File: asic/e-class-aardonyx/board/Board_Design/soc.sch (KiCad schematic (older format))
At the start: 111 parts, among them SW3 SW_DIP_x03, U15 SKT32E

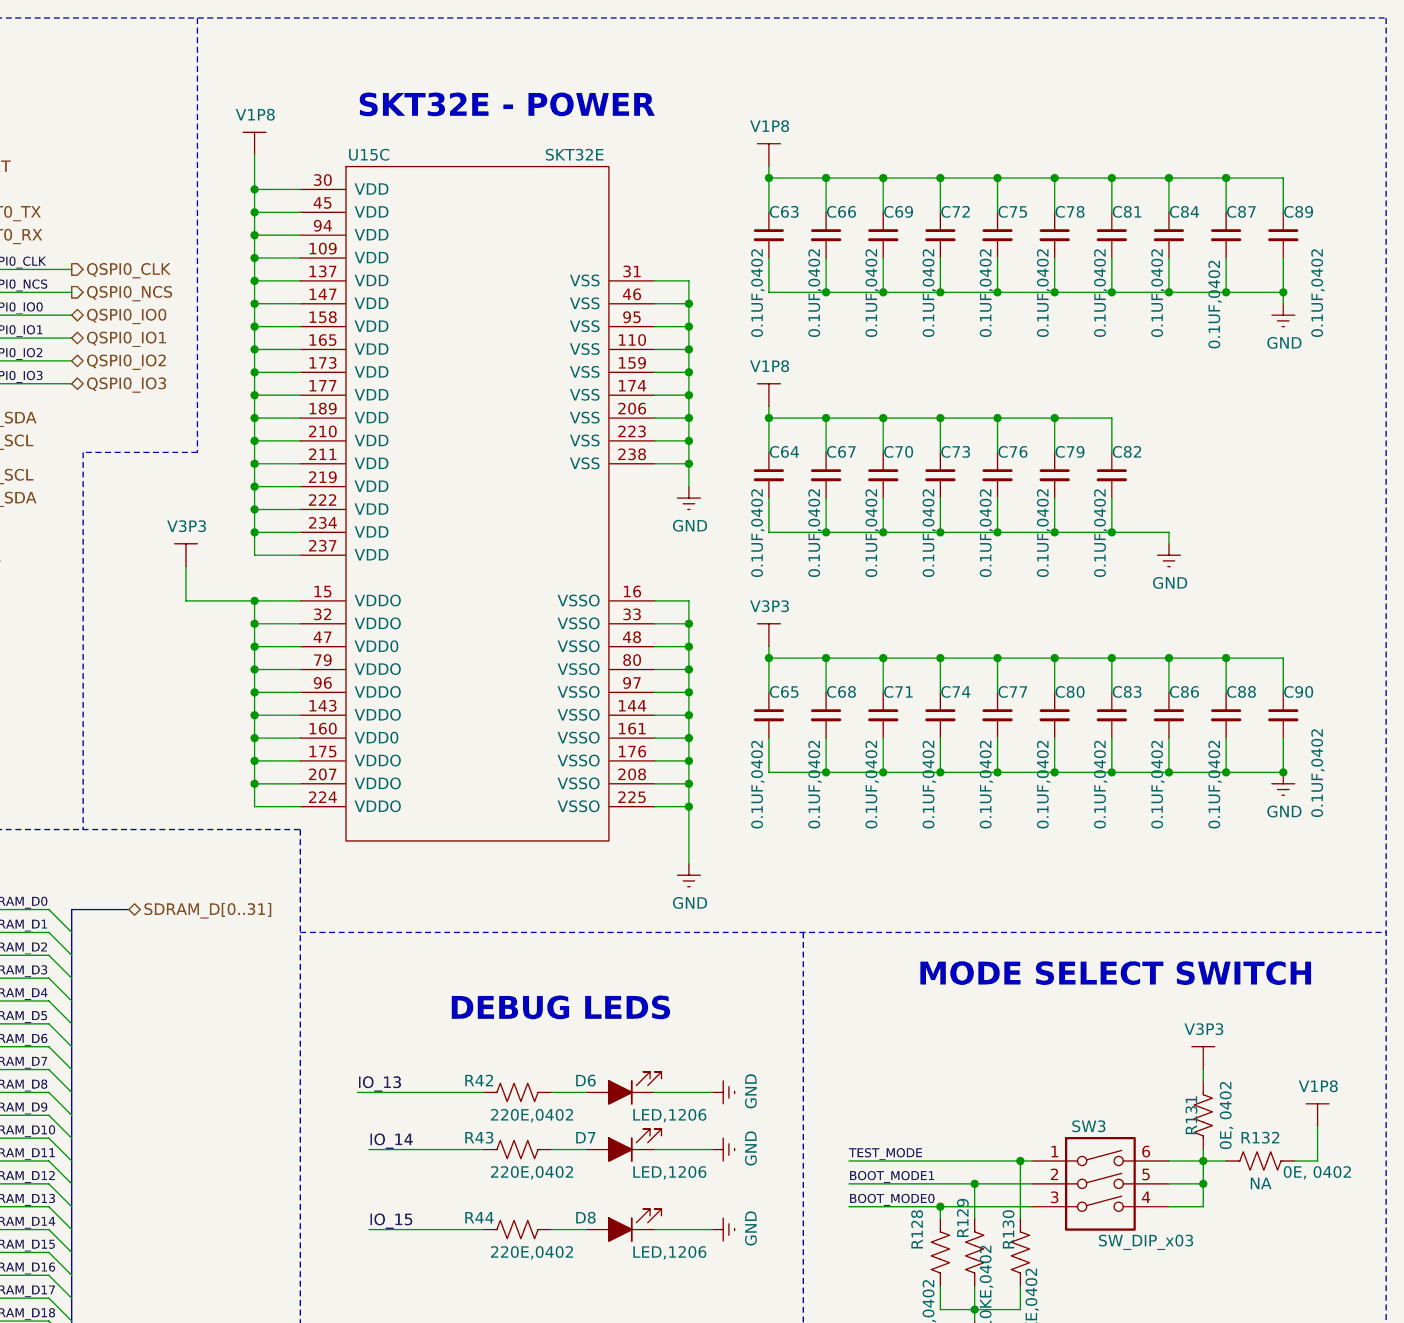
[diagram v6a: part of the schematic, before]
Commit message: Updating 1x6 connector
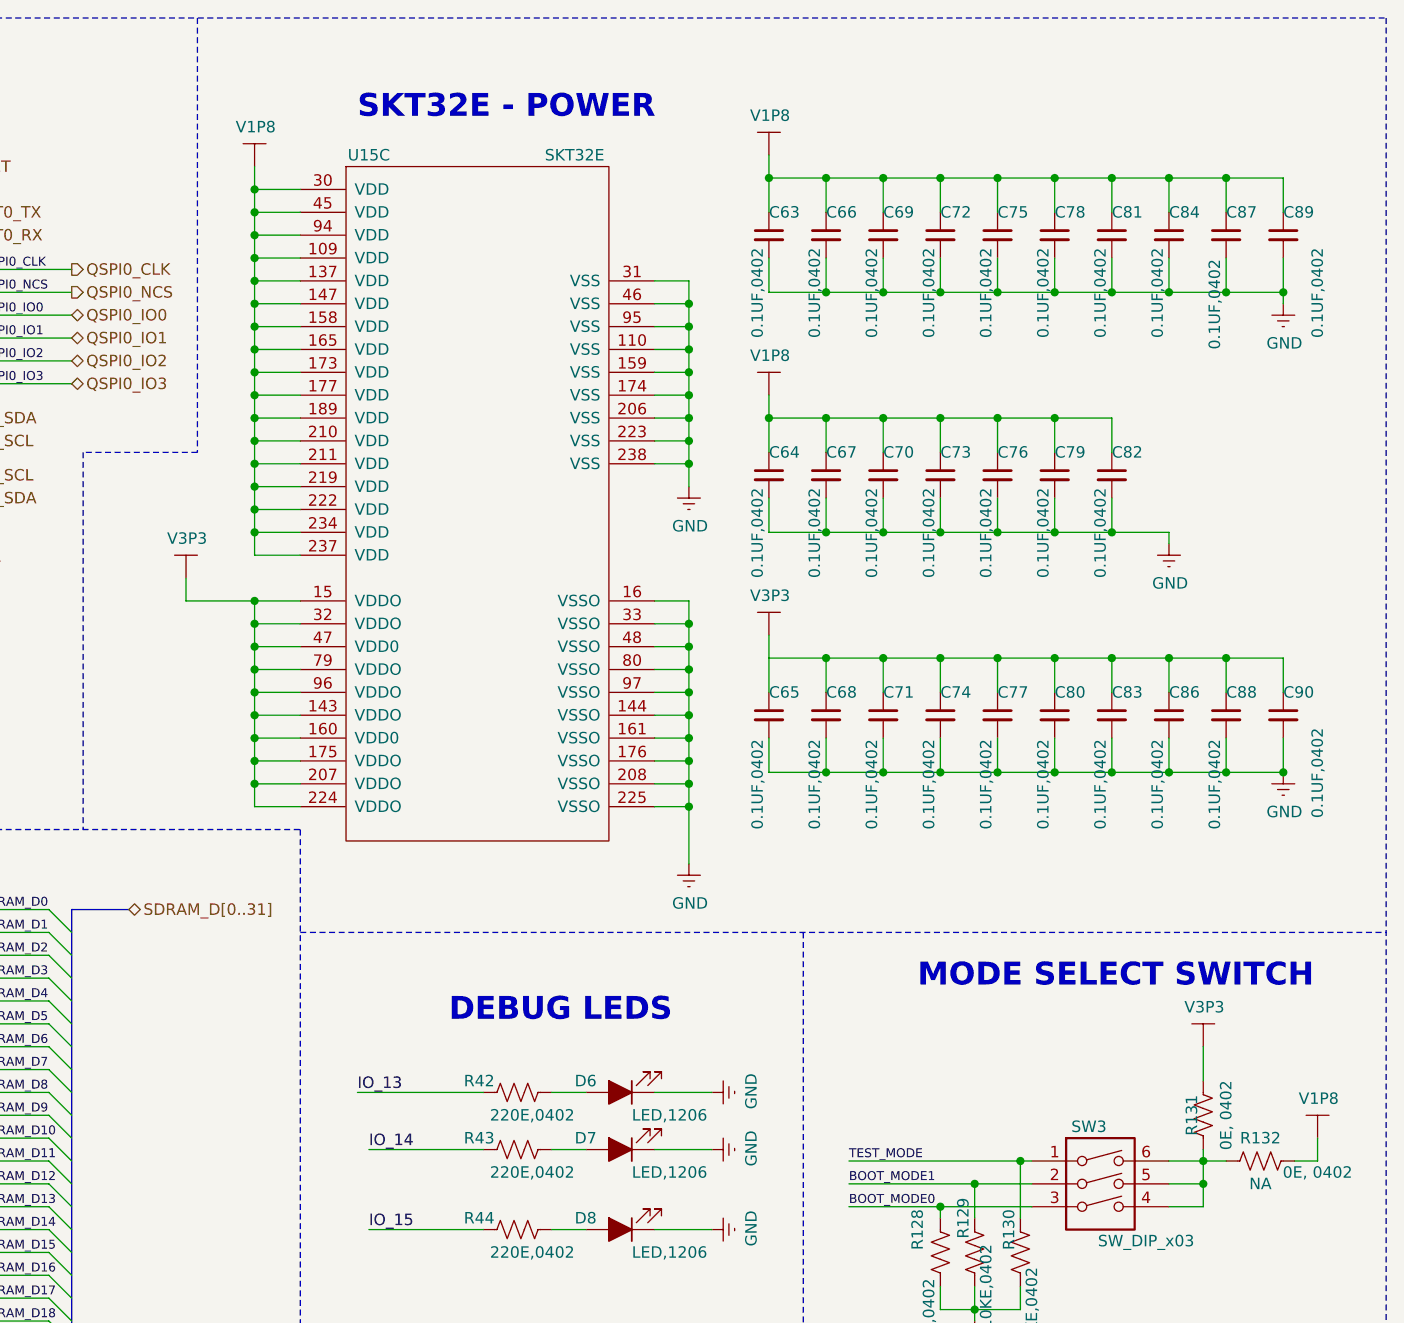
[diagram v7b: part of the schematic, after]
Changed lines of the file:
@@
 EESchema Schematic File Version 4
-EELAYER 30 0
+LIBS:Aardonyx-cache
+EELAYER 29 0
 EELAYER END
 $Descr A4 11693 8268
@@
 Wire Wire Line
 	10250 1550 10250 1700
-Wire Wire Line
-	5950 2900 5950 3050
-$Comp
-L Aardonyx-rescue:V1P8-aardonyx #PWR0128
-U 1 1 5DD1AD11
-P 6250 1100
-F 0 "#PWR0128" H 6400 1050 50  0001 C CNN
-F 1 "V1P8" H 6255 1275 50  0000 C CNN
-F 2 "" H 6250 1100 50  0001 C CNN
-F 3 "" H 6250 1100 50  0001 C CNN
-	1    6250 1100
-	1    0    0    -1
-$EndComp
-$Comp
-L Aardonyx-rescue:V3P3-aardonyx #PWR0127
-U 1 1 5DD1B90C
-P 5950 2900
-F 0 "#PWR0127" H 6100 2850 50  0001 C CNN
-F 1 "V3P3" H 5955 3075 50  0000 C CNN
-F 2 "" H 5950 2900 50  0001 C CNN
-F 3 "" H 5950 2900 50  0001 C CNN
-	1    5950 2900
-	1    0    0    -1
-$EndComp
 $Comp
 L Aardonyx-rescue:GND-aardonyx #PWR0132
@@
 	1    0    0    -1
 $EndComp
-$Comp
-L Aardonyx-rescue:V1P8-aardonyx #PWR0134
-U 1 1 5DD7A800
-P 8500 1150
-F 0 "#PWR0134" H 8650 1100 50  0001 C CNN
-F 1 "V1P8" H 8505 1325 50  0000 C CNN
-F 2 "" H 8500 1150 50  0001 C CNN
-F 3 "" H 8500 1150 50  0001 C CNN
-	1    8500 1150
-	1    0    0    -1
-$EndComp
 Wire Notes Line
 	11200 500  11200 6500
@@
 	8500 2750 8750 2750
 Connection ~ 8750 2750
-Wire Wire Line
-	8500 1150 8500 1200
-Connection ~ 8500 1200
 $Comp
 L Aardonyx-rescue:C_Small-aardonyx C65
@@
 Connection ~ 10750 3800
 $Comp
-L Aardonyx-rescue:V3P3-aardonyx #PWR0136
-U 1 1 5F38AD2A
-P 8500 3250
-F 0 "#PWR0136" H 8650 3200 50  0001 C CNN
-F 1 "V3P3" H 8505 3425 50  0000 C CNN
-F 2 "" H 8500 3250 50  0001 C CNN
-F 3 "" H 8500 3250 50  0001 C CNN
-	1    8500 3250
-	1    0    0    -1
-$EndComp
-Wire Wire Line
-	8500 3250 8500 3300
-Connection ~ 8500 3300
-$Comp
 L Aardonyx-rescue:C_Small-aardonyx C70
 U 1 1 5F55509B
@@
 	1    0    0    -1
 $EndComp
-Wire Wire Line
-	6250 1100 6250 1250
 Connection ~ 6250 1450
 Wire Wire Line
@@
 	10750 1700 10750 1750
 Connection ~ 10250 1700
-$Comp
-L Aardonyx-rescue:V1P8-aardonyx #PWR0135
-U 1 1 5F36DBCF
-P 8500 2200
-F 0 "#PWR0135" H 8650 2150 50  0001 C CNN
-F 1 "V1P8" H 8505 2375 50  0000 C CNN
-F 2 "" H 8500 2200 50  0001 C CNN
-F 3 "" H 8500 2200 50  0001 C CNN
-	1    8500 2200
-	1    0    0    -1
-$EndComp
-Wire Wire Line
-	8500 2200 8500 2250
-Connection ~ 8500 2250
 Wire Wire Line
 	5950 3050 6250 3050
@@
 	1    0    0    -1
 $EndComp
-$Comp
-L Aardonyx-rescue:V3P3-aardonyx #PWR0130
-U 1 1 604A31C5
-P 10400 5100
-F 0 "#PWR0130" H 10550 5050 50  0001 C CNN
-F 1 "V3P3" H 10405 5275 50  0000 C CNN
-F 2 "" H 10400 5100 50  0001 C CNN
-F 3 "" H 10400 5100 50  0001 C CNN
-	1    10400 5100
-	1    0    0    -1
-$EndComp
-$Comp
-L Aardonyx-rescue:V1P8-aardonyx #PWR0133
-U 1 1 604D0ACB
-P 10900 5350
-F 0 "#PWR0133" H 11050 5300 50  0001 C CNN
-F 1 "V1P8" H 10905 5525 50  0000 C CNN
-F 2 "" H 10900 5350 50  0001 C CNN
-F 3 "" H 10900 5350 50  0001 C CNN
-	1    10900 5350
-	1    0    0    -1
-$EndComp
 Wire Wire Line
 	10250 5500 10400 5500
@@
 Wire Wire Line
 	10800 5500 10900 5500
-Wire Wire Line
-	10900 5500 10900 5350
 Text Label 8850 5700 0    39   ~ 0
 BOOT_MODE0
@@
 Connection ~ 9250 5700
 Wire Wire Line
-	10400 5100 10400 5150
-Wire Wire Line
 	10400 5450 10400 5500
 Text Notes 9150 4750 0    100  ~ 20
@@
 Wire Wire Line
 	6450 1250 6250 1250
-Connection ~ 6250 1250
 Wire Wire Line
 	6250 1250 6250 1350
@@
 Text Notes 7100 4900 0    100  ~ 20
 DEBUG LEDS\n
+$Comp
+L Aardonyx-rescue:V3P3 #PWR?
+U 1 1 5F3B53F6
+P 5950 2950
+AR Path="/5D8B3761/5F3B53F6" Ref="#PWR?"  Part="1"
+AR Path="/5D8B3740/5F3B53F6" Ref="#PWR0218"  Part="1"
+F 0 "#PWR0218" H 6100 2900 50  0001 C CNN
+F 1 "V3P3" H 5955 3123 50  0000 C CNN
+F 2 "" H 5950 2950 50  0001 C CNN
+F 3 "" H 5950 2950 50  0001 C CNN
+	1    5950 2950
+	1    0    0    -1
+$EndComp
+Wire Wire Line
+	5950 3050 5950 2950
+$Comp
+L Aardonyx-rescue:V3P3 #PWR?
+U 1 1 5F3EEA2A
+P 8500 3200
+AR Path="/5D8B3761/5F3EEA2A" Ref="#PWR?"  Part="1"
+AR Path="/5D8B3740/5F3EEA2A" Ref="#PWR0219"  Part="1"
+F 0 "#PWR0219" H 8650 3150 50  0001 C CNN
+F 1 "V3P3" H 8505 3373 50  0000 C CNN
+F 2 "" H 8500 3200 50  0001 C CNN
+F 3 "" H 8500 3200 50  0001 C CNN
+	1    8500 3200
+	1    0    0    -1
+$EndComp
+Wire Wire Line
+	8500 3300 8500 3200
+$Comp
+L Aardonyx-rescue:V3P3 #PWR?
+U 1 1 5F427C1A
+P 10400 5000
+AR Path="/5D8B3761/5F427C1A" Ref="#PWR?"  Part="1"
+AR Path="/5D8B3740/5F427C1A" Ref="#PWR0220"  Part="1"
+F 0 "#PWR0220" H 10550 4950 50  0001 C CNN
+F 1 "V3P3" H 10405 5173 50  0000 C CNN
+F 2 "" H 10400 5000 50  0001 C CNN
+F 3 "" H 10400 5000 50  0001 C CNN
+	1    10400 5000
+	1    0    0    -1
+$EndComp
+Wire Wire Line
+	10400 5000 10400 5150
+$Comp
+L Aardonyx-rescue:V1P8 #PWR?
+U 1 1 5F4CC7A5
+P 6250 1150
+AR Path="/5D8B37B8/5F4CC7A5" Ref="#PWR?"  Part="1"
+AR Path="/5D8B3740/5F4CC7A5" Ref="#PWR0221"  Part="1"
+F 0 "#PWR0221" H 6400 1100 50  0001 C CNN
+F 1 "V1P8" H 6255 1323 50  0000 C CNN
+F 2 "" H 6250 1150 50  0001 C CNN
+F 3 "" H 6250 1150 50  0001 C CNN
+	1    6250 1150
+	1    0    0    -1
+$EndComp
+Wire Wire Line
+	6250 1250 6250 1150
+Connection ~ 6250 1250
+$Comp
+L Aardonyx-rescue:V1P8 #PWR?
+U 1 1 5F508AB9
+P 8500 1100
+AR Path="/5D8B37B8/5F508AB9" Ref="#PWR?"  Part="1"
+AR Path="/5D8B3740/5F508AB9" Ref="#PWR0222"  Part="1"
+F 0 "#PWR0222" H 8650 1050 50  0001 C CNN
+F 1 "V1P8" H 8505 1273 50  0000 C CNN
+F 2 "" H 8500 1100 50  0001 C CNN
+F 3 "" H 8500 1100 50  0001 C CNN
+	1    8500 1100
+	1    0    0    -1
+$EndComp
+Wire Wire Line
+	8500 1200 8500 1100
+Connection ~ 8500 1200
+$Comp
+L Aardonyx-rescue:V1P8 #PWR?
+U 1 1 5F54440D
+P 8500 2150
+AR Path="/5D8B37B8/5F54440D" Ref="#PWR?"  Part="1"
+AR Path="/5D8B3740/5F54440D" Ref="#PWR0223"  Part="1"
+F 0 "#PWR0223" H 8650 2100 50  0001 C CNN
+F 1 "V1P8" H 8505 2323 50  0000 C CNN
+F 2 "" H 8500 2150 50  0001 C CNN
+F 3 "" H 8500 2150 50  0001 C CNN
+	1    8500 2150
+	1    0    0    -1
+$EndComp
+Wire Wire Line
+	8500 2250 8500 2150
+Connection ~ 8500 2250
+$Comp
+L Aardonyx-rescue:V1P8 #PWR?
+U 1 1 5F5BB343
+P 10900 5400
+AR Path="/5D8B37B8/5F5BB343" Ref="#PWR?"  Part="1"
+AR Path="/5D8B3740/5F5BB343" Ref="#PWR0224"  Part="1"
+F 0 "#PWR0224" H 11050 5350 50  0001 C CNN
+F 1 "V1P8" H 10905 5573 50  0000 C CNN
+F 2 "" H 10900 5400 50  0001 C CNN
+F 3 "" H 10900 5400 50  0001 C CNN
+	1    10900 5400
+	1    0    0    -1
+$EndComp
+Wire Wire Line
+	10900 5500 10900 5400
 Wire Bus Line
 	1250 5800 1250 6350
